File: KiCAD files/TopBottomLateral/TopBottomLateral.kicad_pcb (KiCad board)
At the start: 2 copper layers, 69.8 x 106.7 mm, 10 parts

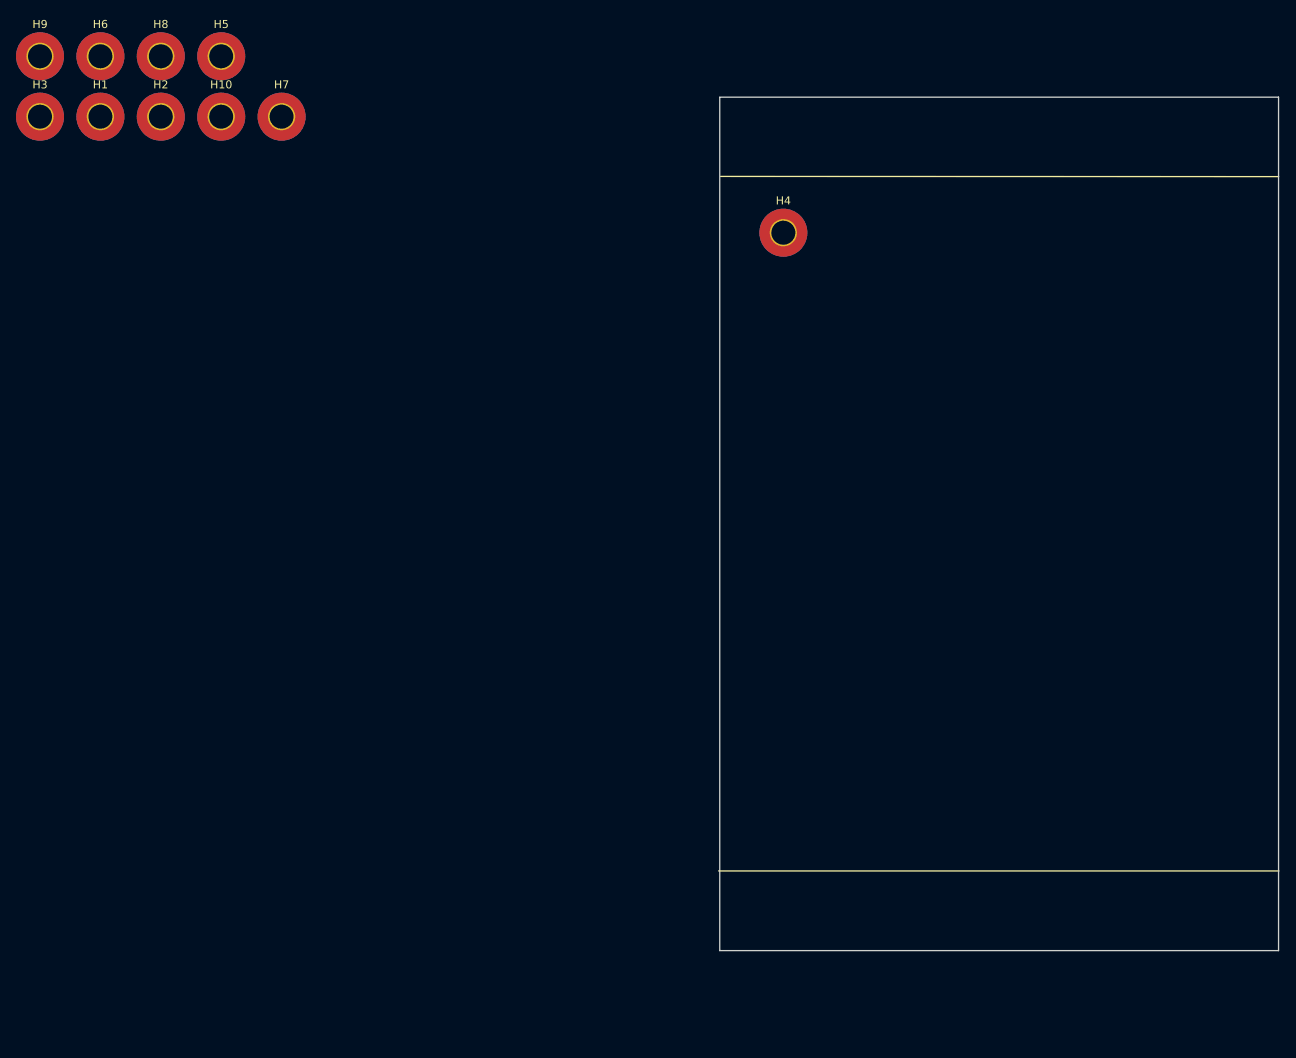
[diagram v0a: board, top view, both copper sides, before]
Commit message: enclosure updates
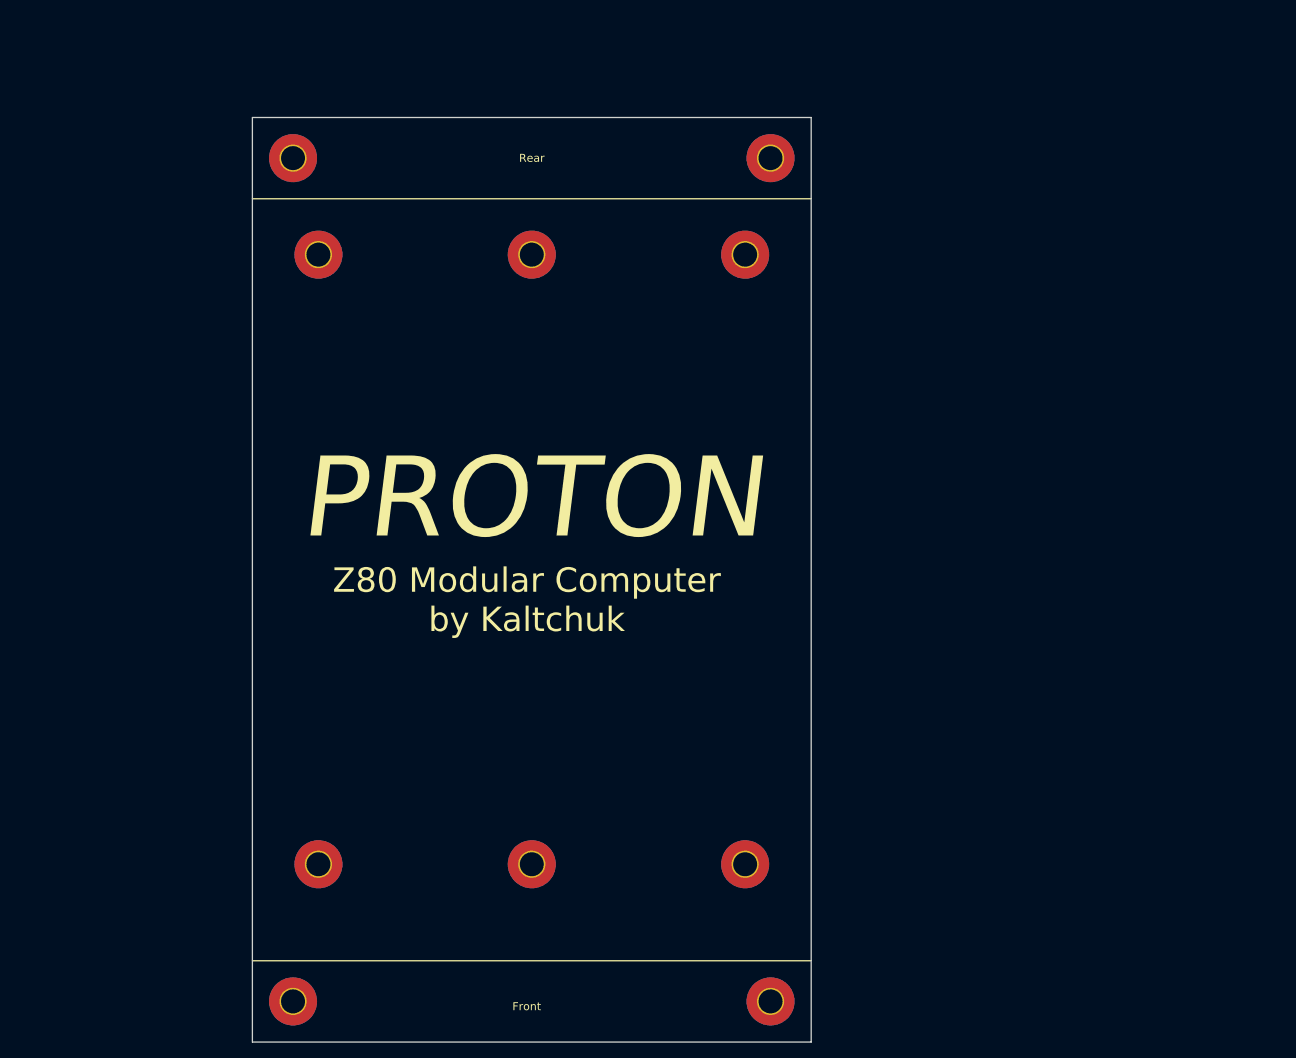
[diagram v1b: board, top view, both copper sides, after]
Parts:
- moved H9 118.2 mm to (93.3, 130.2)
- moved H3 115.0 mm to (63.5, 147.3)
- moved H10 114.1 mm to (120.0, 130.2)
- moved H8 102.9 mm to (66.7, 130.2)
- moved H4 96.1 mm to (123.2, 147.3)
- moved H2 76.4 mm to (123.2, 41.9)
- moved H7 60.5 mm to (120.0, 54.0)
- moved H6 59.4 mm to (93.3, 54.0)
- moved H5 27.6 mm to (66.7, 54.0)
- moved H1 24.6 mm to (63.5, 41.9)
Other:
- board size 69.8 x 106.7 mm -> 69.9 x 115.6 mm
- board text added: "Card slot"
- board text added: "Front"
- board text added: "PROTON"
- board text added: "Rear"
- board text added: "Z80 Modular Computer by Kaltchuk"

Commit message: pcb update
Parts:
- moved H3 8.25 mm to (63.5, 139.1)
- moved H4 8.25 mm to (123.2, 139.1)
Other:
- board size 69.9 x 115.6 mm -> 69.9 x 107.3 mm
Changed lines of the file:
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@@
       (effects (font (size 1 1) (thickness 0.15)))
     )
-    (fp_text value "MountingHole" (at 0 4) (layer "F.Fab")
+    (fp_text value "MountingHole" (at 0 4) (layer "F.Fab") hide
       (effects (font (size 1 1) (thickness 0.15)))
     )
@@
       (effects (font (size 1 1) (thickness 0.15)))
     )
-    (fp_text value "MountingHole" (at 0 4) (layer "F.Fab")
+    (fp_text value "MountingHole" (at 0 4) (layer "F.Fab") hide
       (effects (font (size 1 1) (thickness 0.15)))
     )
@@
       (effects (font (size 1 1) (thickness 0.15)))
     )
-    (fp_text value "MountingHole" (at 0 4) (layer "F.Fab")
+    (fp_text value "MountingHole" (at 0 4) (layer "F.Fab") hide
       (effects (font (size 1 1) (thickness 0.15)))
     )
@@
       (effects (font (size 1 1) (thickness 0.15)))
     )
-    (fp_text value "MountingHole" (at 0 4) (layer "F.Fab")
+    (fp_text value "MountingHole" (at 0 4) (layer "F.Fab") hide
       (effects (font (size 1 1) (thickness 0.15)))
     )
@@
       (effects (font (size 1 1) (thickness 0.15)))
     )
-    (fp_text value "MountingHole" (at 0 4) (layer "F.Fab")
+    (fp_text value "MountingHole" (at 0 4) (layer "F.Fab") hide
       (effects (font (size 1 1) (thickness 0.15)))
     )
@@
       (effects (font (size 1 1) (thickness 0.15)))
     )
-    (fp_text value "MountingHole" (at 0 4) (layer "F.Fab")
+    (fp_text value "MountingHole" (at 0 4) (layer "F.Fab") hide
       (effects (font (size 1 1) (thickness 0.15)))
     )
@@
       (effects (font (size 1 1) (thickness 0.15)))
     )
-    (fp_text value "MountingHole" (at 0 4) (layer "F.Fab")
+    (fp_text value "MountingHole" (at 0 4) (layer "F.Fab") hide
       (effects (font (size 1 1) (thickness 0.15)))
     )
@@
       (effects (font (size 1 1) (thickness 0.15)))
     )
-    (fp_text value "MountingHole" (at 0 4) (layer "F.Fab")
-      (effects (font (size 1 1) (thickness 0.15)))
-    )
-    (fp_text user "${REFERENCE}" (at 0 0) (layer "F.Fab")
-      (effects (font (size 1 1) (thickness 0.15)))
-    )
-    (fp_circle (center 0 0) (end 3 0) (layer "Cmts.User") (width 0.15) (fill none))
-    (fp_circle (center 0 0) (end 3.25 0) (layer "F.CrtYd") (width 0.05) (fill none))
-    (pad "1" thru_hole circle (at 0 0) (size 3.4 3.4) (drill 3) (layers *.Cu *.Mask))
-    (pad "1" connect circle (at 0 0) (size 6 6) (layers "F.Cu" "F.Mask"))
-    (pad "1" connect circle (at 0 0) (size 6 6) (layers "B.Cu" "B.Mask"))
-  )
-  (footprint "MountingHole:MountingHole_3mm_Pad_TopBottom" (layer "F.Cu")
-    (at 63.5 147.32)
+    (fp_text value "MountingHole" (at 0 4) (layer "F.Fab") hide
+      (effects (font (size 1 1) (thickness 0.15)))
+    )
+    (fp_text user "${REFERENCE}" (at 0 0) (layer "F.Fab")
+      (effects (font (size 1 1) (thickness 0.15)))
+    )
+    (fp_circle (center 0 0) (end 3 0) (layer "Cmts.User") (width 0.15) (fill none))
+    (fp_circle (center 0 0) (end 3.25 0) (layer "F.CrtYd") (width 0.05) (fill none))
+    (pad "1" thru_hole circle (at 0 0) (size 3.4 3.4) (drill 3) (layers *.Cu *.Mask))
+    (pad "1" connect circle (at 0 0) (size 6 6) (layers "F.Cu" "F.Mask"))
+    (pad "1" connect circle (at 0 0) (size 6 6) (layers "B.Cu" "B.Mask"))
+  )
+  (footprint "MountingHole:MountingHole_3mm_Pad_TopBottom" (layer "F.Cu")
+    (at 63.5 139.065)
     (descr "Mounting Hole 3mm")
     (tags "mounting hole 3mm")
@@
       (effects (font (size 1 1) (thickness 0.15)))
     )
-    (fp_text value "MountingHole" (at 0 4) (layer "F.Fab")
-      (effects (font (size 1 1) (thickness 0.15)))
-    )
-    (fp_text user "${REFERENCE}" (at 0 0) (layer "F.Fab")
-      (effects (font (size 1 1) (thickness 0.15)))
-    )
-    (fp_circle (center 0 0) (end 3 0) (layer "Cmts.User") (width 0.15) (fill none))
-    (fp_circle (center 0 0) (end 3.25 0) (layer "F.CrtYd") (width 0.05) (fill none))
-    (pad "1" thru_hole circle (at 0 0) (size 3.4 3.4) (drill 3) (layers *.Cu *.Mask))
-    (pad "1" connect circle (at 0 0) (size 6 6) (layers "B.Cu" "B.Mask"))
-    (pad "1" connect circle (at 0 0) (size 6 6) (layers "F.Cu" "F.Mask"))
-  )
-  (footprint "MountingHole:MountingHole_3mm_Pad_TopBottom" (layer "F.Cu")
-    (at 123.19 147.32)
+    (fp_text value "MountingHole" (at 0 4) (layer "F.Fab") hide
+      (effects (font (size 1 1) (thickness 0.15)))
+    )
+    (fp_text user "${REFERENCE}" (at 0 0) (layer "F.Fab")
+      (effects (font (size 1 1) (thickness 0.15)))
+    )
+    (fp_circle (center 0 0) (end 3 0) (layer "Cmts.User") (width 0.15) (fill none))
+    (fp_circle (center 0 0) (end 3.25 0) (layer "F.CrtYd") (width 0.05) (fill none))
+    (pad "1" thru_hole circle (at 0 0) (size 3.4 3.4) (drill 3) (layers *.Cu *.Mask))
+    (pad "1" connect circle (at 0 0) (size 6 6) (layers "B.Cu" "B.Mask"))
+    (pad "1" connect circle (at 0 0) (size 6 6) (layers "F.Cu" "F.Mask"))
+  )
+  (footprint "MountingHole:MountingHole_3mm_Pad_TopBottom" (layer "F.Cu")
+    (at 123.19 139.065)
     (descr "Mounting Hole 3mm")
     (tags "mounting hole 3mm")
@@
       (effects (font (size 1 1) (thickness 0.15)))
     )
-    (fp_text value "MountingHole" (at 0 4) (layer "F.Fab")
-      (effects (font (size 1 1) (thickness 0.15)))
-    )
-    (fp_text user "${REFERENCE}" (at 0 0) (layer "F.Fab")
-      (effects (font (size 1 1) (thickness 0.15)))
-    )
-    (fp_circle (center 0 0) (end 3 0) (layer "Cmts.User") (width 0.15) (fill none))
-    (fp_circle (center 0 0) (end 3.25 0) (layer "F.CrtYd") (width 0.05) (fill none))
-    (pad "1" connect circle (at 0 0) (size 6 6) (layers "F.Cu" "F.Mask"))
-    (pad "1" connect circle (at 0 0) (size 6 6) (layers "B.Cu" "B.Mask"))
-    (pad "1" thru_hole circle (at 0 0) (size 3.4 3.4) (drill 3) (layers *.Cu *.Mask))
-  )
-  (gr_line (start 93.345 60.325) (end 93.345 125.73) (layer "B.SilkS") (width 0.3048))
-  (gr_line (start 66.675 60.325) (end 66.675 125.73) (layer "B.SilkS") (width 0.3048))
-  (gr_line (start 120.015 60.325) (end 120.015 125.73) (layer "B.SilkS") (width 0.3048))
-  (gr_line (start 128.27 142.24) (end 58.42 142.24) (layer "F.SilkS") (width 0.15))
+    (fp_text value "MountingHole" (at 0 4) (layer "F.Fab") hide
+      (effects (font (size 1 1) (thickness 0.15)))
+    )
+    (fp_text user "${REFERENCE}" (at 0 0) (layer "F.Fab")
+      (effects (font (size 1 1) (thickness 0.15)))
+    )
+    (fp_circle (center 0 0) (end 3 0) (layer "Cmts.User") (width 0.15) (fill none))
+    (fp_circle (center 0 0) (end 3.25 0) (layer "F.CrtYd") (width 0.05) (fill none))
+    (pad "1" connect circle (at 0 0) (size 6 6) (layers "F.Cu" "F.Mask"))
+    (pad "1" connect circle (at 0 0) (size 6 6) (layers "B.Cu" "B.Mask"))
+    (pad "1" thru_hole circle (at 0 0) (size 3.4 3.4) (drill 3) (layers *.Cu *.Mask))
+  )
+  (gr_line (start 93.345 58.42) (end 93.345 125.73) (layer "B.SilkS") (width 0.3048))
+  (gr_line (start 66.675 58.42) (end 66.675 125.73) (layer "B.SilkS") (width 0.3048))
+  (gr_line (start 120.015 58.42) (end 120.015 125.73) (layer "B.SilkS") (width 0.3048))
+  (gr_line (start 128.27 133.985) (end 58.42 133.985) (layer "F.SilkS") (width 0.15))
   (gr_line (start 128.27 46.99) (end 58.42 46.99) (layer "F.SilkS") (width 0.15))
-  (gr_line (start 58.42 152.4) (end 58.42 36.83) (layer "Edge.Cuts") (width 0.1))
+  (gr_line (start 58.42 144.145) (end 58.42 36.83) (layer "Edge.Cuts") (width 0.1))
   (gr_line (start 58.42 36.83) (end 128.27 36.83) (layer "Edge.Cuts") (width 0.1))
-  (gr_line (start 128.27 152.4) (end 128.27 36.83) (layer "Edge.Cuts") (width 0.1))
-  (gr_line (start 58.42 152.4) (end 128.27 152.4) (layer "Edge.Cuts") (width 0.1))
+  (gr_line (start 128.27 144.145) (end 128.27 36.83) (layer "Edge.Cuts") (width 0.1))
+  (gr_line (start 58.42 144.145) (end 128.27 144.145) (layer "Edge.Cuts") (width 0.1))
   (gr_text "Card slot" (at 118.745 90.805 90) (layer "B.SilkS")
     (effects (font (size 1 1) (thickness 0.15)) (justify mirror))
@@
     (effects (font (size 3.048 3.048) (thickness 0.4572)))
   )
-  (gr_text "Front" (at 92.71 147.955) (layer "F.SilkS")
+  (gr_text "Front" (at 93.345 139.7) (layer "F.SilkS")
     (effects (font (size 1 1) (thickness 0.15)))
   )

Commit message: i2c manager fix
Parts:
- moved H3 8.89 mm to (72.4, 139.1)
- moved H4 8.89 mm to (114.3, 139.1)
- moved H2 6.35 mm to (116.8, 41.9)
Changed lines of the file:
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@@
   )
   (footprint "MountingHole:MountingHole_3mm_Pad_TopBottom" (layer "F.Cu")
-    (at 123.19 41.91)
+    (at 116.84 41.91)
     (descr "Mounting Hole 3mm")
     (tags "mounting hole 3mm")
@@
   )
   (footprint "MountingHole:MountingHole_3mm_Pad_TopBottom" (layer "F.Cu")
-    (at 63.5 139.065)
+    (at 72.39 139.065)
     (descr "Mounting Hole 3mm")
     (tags "mounting hole 3mm")
@@
   )
   (footprint "MountingHole:MountingHole_3mm_Pad_TopBottom" (layer "F.Cu")
-    (at 123.19 139.065)
+    (at 114.3 139.065)
     (descr "Mounting Hole 3mm")
     (tags "mounting hole 3mm")

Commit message: PCBs
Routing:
- added copper zone on B.Cu, net (none)
- added copper zone on F.Cu, net (none)
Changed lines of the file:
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@@
     (pad_to_mask_clearance 0)
     (pcbplotparams
-      (layerselection 0x00010fc_ffffffff)
+      (layerselection 0x00010f0_ffffffff)
       (disableapertmacros false)
       (usegerberextensions false)
@@
       (outputformat 1)
       (mirror false)
-      (drillshape 1)
+      (drillshape 0)
       (scaleselection 1)
       (outputdirectory "")
@@
     (effects (font (size 1 1) (thickness 0.15)))
   )
+  (zone (net 0) (net_name "") (layers F&B.Cu) (hatch edge 0.508)
+    (connect_pads (clearance 0.508))
+    (min_thickness 0.254) (filled_areas_thickness no)
+    (fill yes (thermal_gap 0.508) (thermal_bridge_width 0.508))
+    (polygon
+      (pts
+        (xy 128.27 144.145)
+        (xy 58.42 144.145)
+        (xy 58.42 36.83)
+        (xy 128.27 36.703)
+      )
+    )
+  )
 )
